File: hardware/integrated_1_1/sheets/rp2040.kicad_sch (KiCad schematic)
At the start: 27 parts, among them SW1 DNF, SW2 DNF, U11 FT2404A, U7 W25Q16JV, U8 RP2040, Y1 12MHz

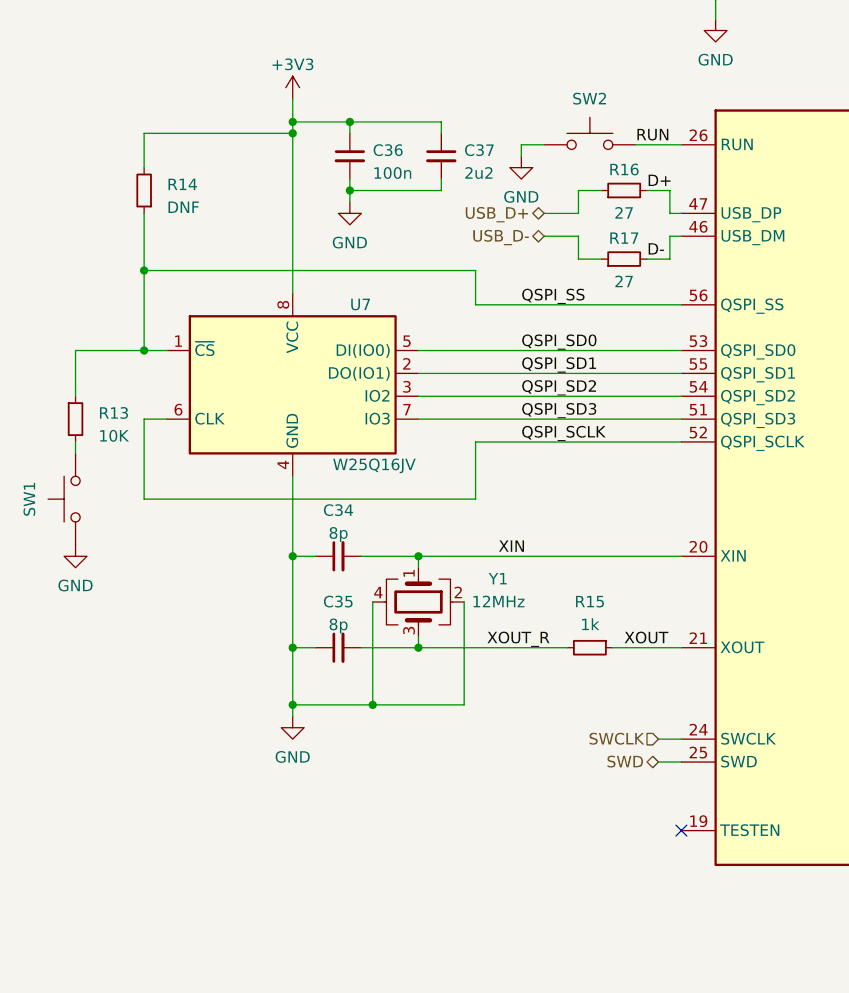
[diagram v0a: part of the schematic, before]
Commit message: implemented changes as suggested by https://github.com/diminDDL
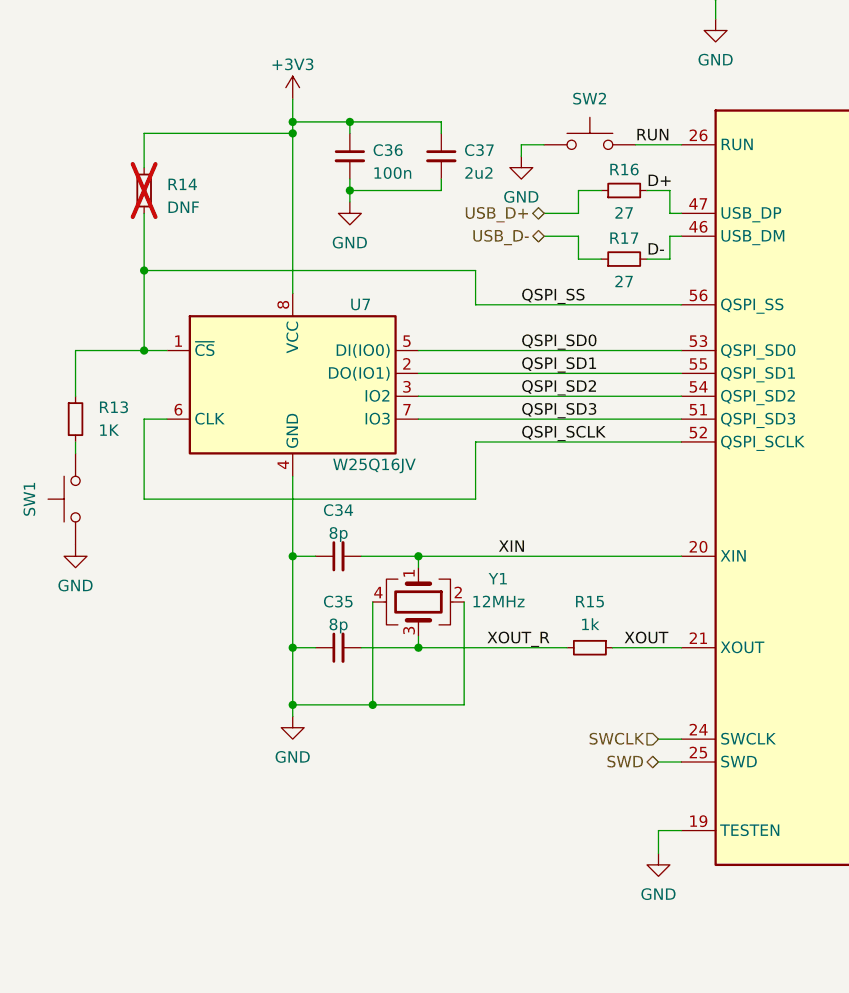
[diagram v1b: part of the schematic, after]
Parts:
- R13: value 10K -> 1K
- R14: now not fitted
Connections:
- net GND: now also U8.19 (TESTEN)
- no-connect marks 12 -> 11
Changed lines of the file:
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@@
 	)
 	(no_connect
-		(at 123.19 147.32)
-	)
-	(no_connect
 		(at 173.99 106.68)
 	)
@@
 	(wire
 		(pts
+			(xy 120.65 147.32) (xy 123.19 147.32)
+		)
+		(stroke
+			(width 0)
+			(type default)
+		)
+	)
+	(wire
+		(pts
 			(xy 154.94 44.45) (xy 154.94 46.99)
 		)
@@
 	(wire
 		(pts
+			(xy 120.65 149.86) (xy 120.65 147.32)
+		)
+		(stroke
+			(width 0)
+			(type default)
+		)
+	)
+	(wire
+		(pts
 			(xy 80.01 134.62) (xy 80.01 133.35)
 		)
@@
 	)
 	(symbol
+		(lib_id "power:GND")
+		(at 120.65 149.86 0)
+		(unit 1)
+		(exclude_from_sim no)
+		(in_bom yes)
+		(on_board yes)
+		(dnp no)
+		(fields_autoplaced yes)
+		(property "Reference" "#PWR031"
+			(at 120.65 156.21 0)
+			(effects
+				(font
+					(size 1.27 1.27)
+				)
+				(hide yes)
+			)
+		)
+		(property "Value" "GND"
+			(at 120.65 154.4225 0)
+			(effects
+				(font
+					(size 1.27 1.27)
+				)
+			)
+		)
+		(property "Footprint" ""
+			(at 120.65 149.86 0)
+			(effects
+				(font
+					(size 1.27 1.27)
+				)
+				(hide yes)
+			)
+		)
+		(property "Datasheet" ""
+			(at 120.65 149.86 0)
+			(effects
+				(font
+					(size 1.27 1.27)
+				)
+				(hide yes)
+			)
+		)
+		(property "Description" ""
+			(at 120.65 149.86 0)
+			(effects
+				(font
+					(size 1.27 1.27)
+				)
+				(hide yes)
+			)
+		)
+		(pin "1"
+		)
+		(instances
+			(project "integrated"
+				(path "/5cc60e42-d666-4a43-b4f0-3784ee4bf951/19012e16-7cd6-4497-8667-921149ac83fb"
+					(reference "#PWR031")
+					(unit 1)
+				)
+			)
+		)
+	)
+	(symbol
 		(lib_id "Device:C_Small")
 		(at 163.83 49.53 0)
@@
 		(in_bom yes)
 		(on_board yes)
-		(dnp no)
+		(dnp yes)
 		(fields_autoplaced yes)
 		(property "Reference" "R14"
@@
 		(fields_autoplaced yes)
 		(property "Reference" "R13"
-			(at 58.42 100.965 0)
+			(at 58.42 100.3299 0)
 			(effects
 				(font
@@
 			)
 		)
-		(property "Value" "10K"
-			(at 58.42 103.505 0)
+		(property "Value" "1K"
+			(at 58.42 102.8699 0)
 			(effects
 				(font
